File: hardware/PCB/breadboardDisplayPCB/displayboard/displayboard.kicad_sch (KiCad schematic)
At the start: 46 parts, among them J1 Conn_01x09_Socket, Q1 2N7000, U1 74HC595, U2 74HC595, U3 74HC595, U4 74HC595, U5 74HC595, U6 TBD62783A, U7 TBD62783A, U8 ULN2803A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

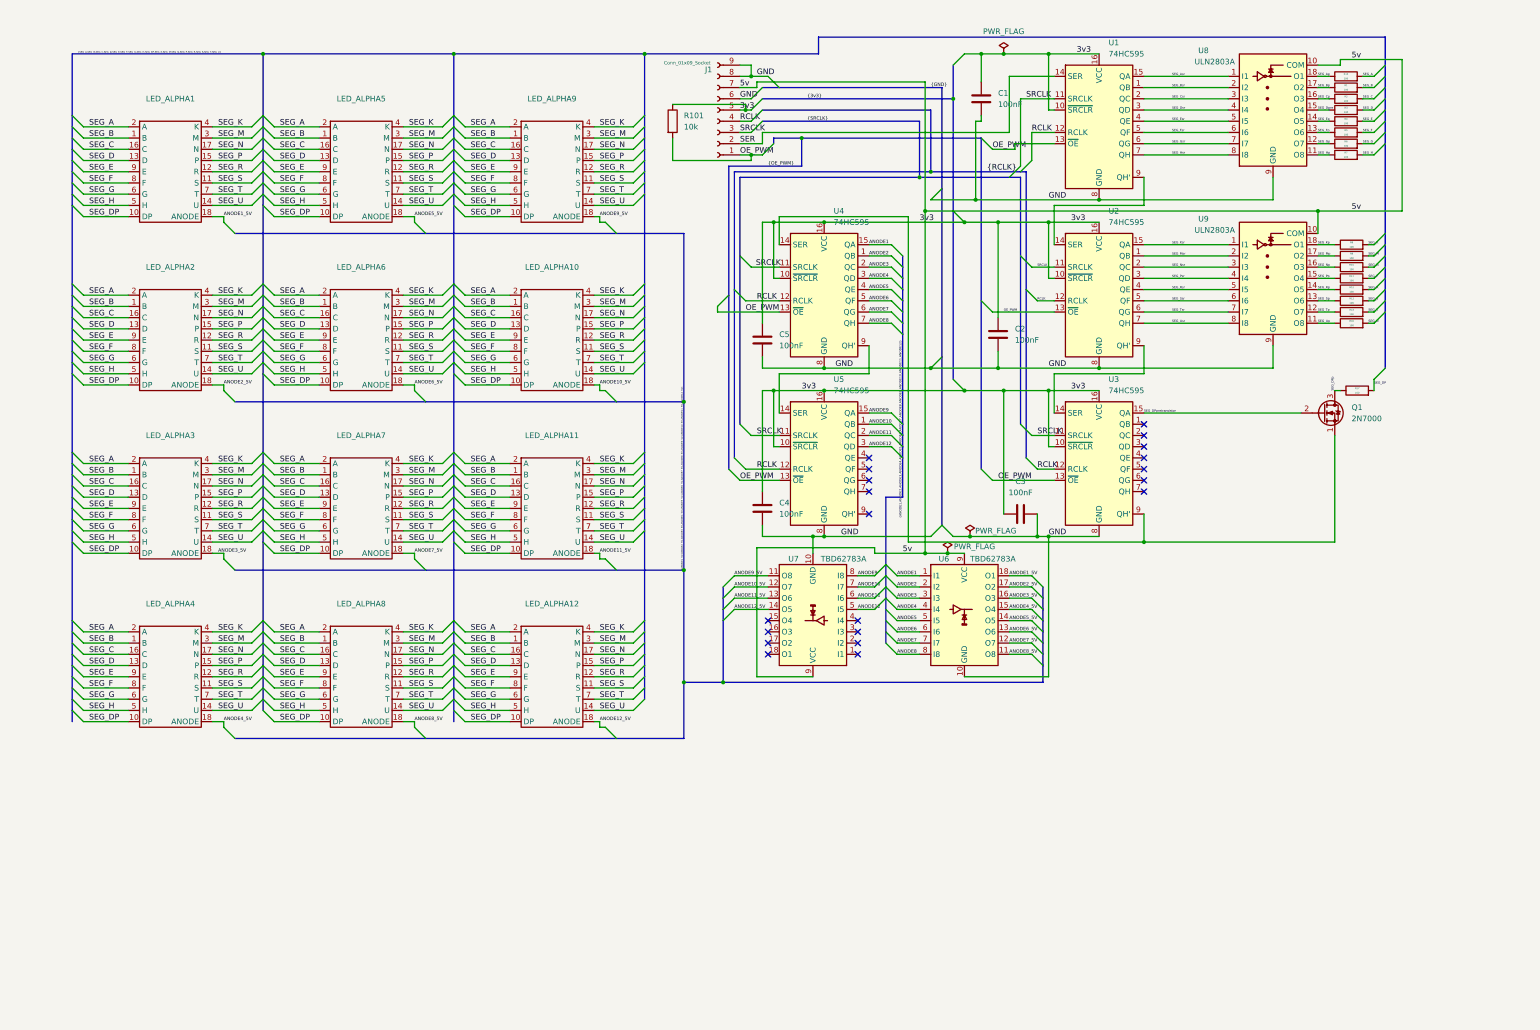
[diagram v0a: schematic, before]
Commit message: begin work on final display PCB
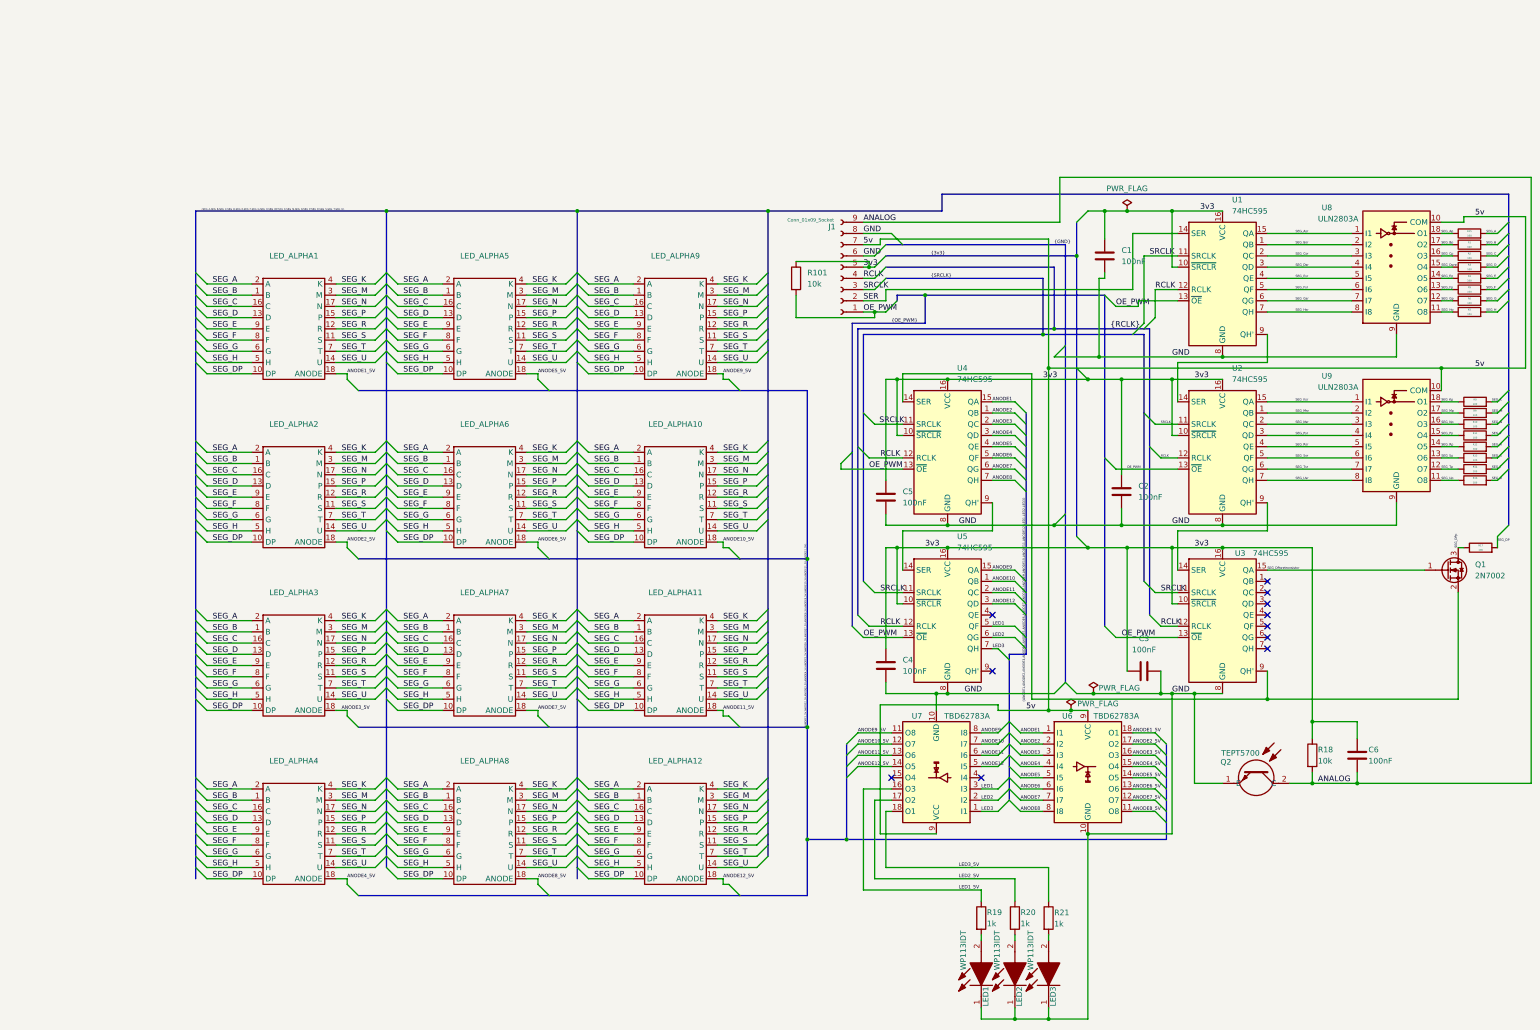
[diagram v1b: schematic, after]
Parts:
- removed Q1: 2N7000, Package_TO_SOT_THT:TO-92_Inline, symbol Transistor_FET:2N7000
- added C6: 100nF, Capacitor_SMD:C_0603_1608Metric, symbol Device:C
- added LED1, LED2, LED3: WP113IDT, SamacSys_Parts:WP113IDT, symbol SamacSys_Parts:WP113IDT
- added Q1: 2N7002, Package_TO_SOT_SMD:SOT-23, symbol Transistor_FET:2N7002
- added Q2: TEPT5700, SamacSys_Parts:TEPT5700, symbol SamacSys_Parts:TEPT5700
- added R18: 10k, Resistor_SMD:R_0805_2012Metric, symbol Device:R
- added R19, R20, R21: 1k, Resistor_SMD:R_0603_1608Metric, symbol Device:R
- C1, C2, C3, C4, C5: footprint Capacitor_THT:C_Disc_D5.0mm_W2.5mm_P5.00mm -> Capacitor_SMD:C_0603_1608Metric
- J1: footprint Connector_PinHeader_2.54mm:PinHeader_1x09_P2.54mm_Vertical -> Connector_JST:JST_XH_B9B-XH-A_1x09_P2.50mm_Vertical
- R1, R10, R11, R12, R13, R14, R15, R16, R17, R2, R3, R4, R5, R6, R7, R8, R9: footprint Resistor_THT:R_Axial_DIN0207_L6.3mm_D2.5mm_P7.62mm_Horizontal -> Resistor_SMD:R_0805_2012Metric
- R101: footprint Resistor_THT:R_Axial_DIN0207_L6.3mm_D2.5mm_P7.62mm_Horizontal -> Resistor_SMD:R_0603_1608Metric
- U1, U2, U3, U4, U5: footprint Package_DIP:DIP-16_W7.62mm_Socket -> Package_SO:SOIC-16_3.9x9.9mm_P1.27mm
- U6, U7, U8, U9: footprint Package_DIP:DIP-18_W7.62mm_Socket -> Package_SO:SOIC-18W_7.5x11.6mm_P1.27mm
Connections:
- net 3v3: now also C6.1, R18.1
- net GND: now also LED1.1 (K), LED2.1 (K), LED3.1 (K), Q2.1 (E); no longer J1.9 (Pin_9)
- net SEG_DPp: now also Q1.3 (D)
- net SEG_DPpretransistor: now also Q1.1 (G)
- net at U3.9 (QH'), U4.14 (SER): now also Q1.2 (S)
- net LED3: now reaches U7.1 (I1)
- net LED3: now also U5.7 (QH)
- net LED1_5V: now reaches U7.16 (O3)
- net LED1_5V: now also R19.1
- net LED2_5V: now reaches U7.17 (O2)
- net LED2_5V: now also R20.1
- net LED3_5V: now reaches U7.18 (O1)
- net LED3_5V: now also R21.1
- net LED2: now reaches U7.2 (I2)
- net LED2: now also U5.6 (QG)
- net LED1: now reaches U7.3 (I3)
- net LED1: now also U5.5 (QF)
- new net: LED1.2 (A), R19.2
- new net: LED3.2 (A), R21.2
- new net: LED2.2 (A), R20.2
- new net ANALOG: C6.2, J1.9 (Pin_9), Q2.2 (C), R18.2
- no-connect marks 20 -> 11
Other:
- moved on the sheet: C1, C2, C3, C4, C5, J1, LED_ALPHA1, LED_ALPHA10, LED_ALPHA11, LED_ALPHA12, LED_ALPHA2, LED_ALPHA3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

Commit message: final PCB rev work
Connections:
- net GND: now also Q1.2 (S)
- net at U3.9 (QH'), U4.14 (SER): no longer Q1.2 (S)
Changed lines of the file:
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@@
 	)
 	(junction
-		(at 224.79 96.52)
+		(at 287.02 167.64)
 		(diameter 0)
 		(color 0 0 0 0)
 	)
 	(junction
-		(at 260.35 58.42)
+		(at 224.79 96.52)
 		(diameter 0)
 		(color 0 0 0 0)
 	)
 	(junction
-		(at 254 68.58)
+		(at 260.35 58.42)
 		(diameter 0)
 		(color 0 0 0 0)
 	)
 	(junction
-		(at 297.18 168.91)
+		(at 254 68.58)
 		(diameter 0)
 		(color 0 0 0 0)
@@
 	(wire
 		(pts
+			(xy 340.36 144.78) (xy 340.36 167.64)
+		)
+		(stroke
+			(width 0)
+			(type default)
+		)
+	)
+	(wire
+		(pts
 			(xy 264.16 125.73) (xy 264.16 129.54)
 		)
@@
 	(wire
 		(pts
+			(xy 340.36 167.64) (xy 287.02 167.64)
+		)
+		(stroke
+			(width 0)
+			(type default)
+		)
+	)
+	(wire
+		(pts
 			(xy 86.36 74.93) (xy 95.25 74.93)
 		)
@@
 	(wire
 		(pts
-			(xy 297.18 168.91) (xy 340.36 168.91)
-		)
-		(stroke
-			(width 0)
-			(type default)
-		)
-	)
-	(wire
-		(pts
 			(xy 287.02 187.96) (xy 280.67 187.96)
 		)
@@
 		)
 		(stroke
-			(width 0)
-			(type default)
-		)
-	)
-	(wire
-		(pts
-			(xy 340.36 144.78) (xy 340.36 168.91)
-		)
-		(stroke

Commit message: large commit of PCB progress
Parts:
- added C7: 47uF, Capacitor_SMD:CP_Elec_6.3x5.4, symbol Device:C_Polarized
- C1, C2, C3, C6: LCSC (none) -> C14663
- C4: renamed from C5; LCSC (none) -> C14663
- C5: renamed from C4; LCSC (none) -> C14663
- J1, LED1, LED2, LED3, LED_ALPHA1, LED_ALPHA12, Q2: now left out of the parts list
- LED_ALPHA10: renamed from LED_ALPHA4; now left out of the parts list
- LED_ALPHA11: renamed from LED_ALPHA8; now left out of the parts list
- LED_ALPHA2: renamed from LED_ALPHA5; now left out of the parts list
- LED_ALPHA3: renamed from LED_ALPHA9; now left out of the parts list
- LED_ALPHA4: renamed from LED_ALPHA2; now left out of the parts list
- LED_ALPHA5: renamed from LED_ALPHA6; now left out of the parts list
- LED_ALPHA6: renamed from LED_ALPHA10; now left out of the parts list
- LED_ALPHA7: renamed from LED_ALPHA3; now left out of the parts list
- LED_ALPHA8: renamed from LED_ALPHA7; now left out of the parts list
- LED_ALPHA9: renamed from LED_ALPHA11; now left out of the parts list
- Q1: LCSC (none) -> C8545
- R1, R10, R11, R12, R13, R14, R15, R16, R17, R2, R3, R4, R5, R6, R7, R8, R9: LCSC (none) -> C17467
- R101: LCSC (none) -> C25804
- R18: LCSC (none) -> C17414
- R19, R20, R21: LCSC (none) -> C21122
- U1, U2, U3, U4, U5: LCSC (none) -> C14791
- U6, U7: LCSC (none) -> C96336
- U8, U9: value ULN2803A -> TBD62083A; LCSC (none) -> C134547
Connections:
- net ANODE10: now also U7.2 (I2); no longer U7.7 (I7)
- net ANODE10_5V: now also LED_ALPHA10.18 (ANODE), U7.17 (O2); no longer LED_ALPHA6.18 (ANODE), U7.12 (O7)
- net ANODE11: now also U7.3 (I3); no longer U7.6 (I6)
- net ANODE11_5V: now also LED_ALPHA11.18 (ANODE), U7.16 (O3); no longer LED_ALPHA9.18 (ANODE), U7.13 (O6)
- net ANODE12: now also U7.4 (I4); no longer U7.5 (I5)
- net ANODE12_5V: now also U7.15 (O4); no longer U7.14 (O5)
- net ANODE2_5V: now also LED_ALPHA2.18 (ANODE); no longer LED_ALPHA4.18 (ANODE)
- net ANODE3_5V: now also LED_ALPHA3.18 (ANODE); no longer LED_ALPHA7.18 (ANODE)
- net ANODE4_5V: now also LED_ALPHA4.18 (ANODE); no longer LED_ALPHA10.18 (ANODE)
- net ANODE5_5V: now also LED_ALPHA5.18 (ANODE); no longer LED_ALPHA2.18 (ANODE)
- net ANODE6_5V: now also LED_ALPHA6.18 (ANODE); no longer LED_ALPHA5.18 (ANODE)
- net ANODE7_5V: now also LED_ALPHA7.18 (ANODE); no longer LED_ALPHA8.18 (ANODE)
- net ANODE8_5V: now also LED_ALPHA8.18 (ANODE); no longer LED_ALPHA11.18 (ANODE)
- net ANODE9: now also U7.1 (I1); no longer U7.8 (I8)
- net ANODE9_5V: now also LED_ALPHA9.18 (ANODE), U7.18 (O1); no longer LED_ALPHA3.18 (ANODE), U7.11 (O8)
- net GND: now also C2.1, C3.1, C4.2, C5.2, C7.2; no longer C2.2, C3.2, C4.1, C5.1
- net LED1: now also U7.6 (I6); no longer U7.3 (I3)
- net LED1_5V: now also U7.13 (O6); no longer U7.16 (O3)
- net LED2: now also U7.7 (I7); no longer U7.2 (I2)
- net LED2_5V: now also U7.12 (O7); no longer U7.17 (O2)
- net LED3: now also U7.8 (I8); no longer U7.1 (I1)
- net LED3_5V: now also U7.11 (O8); no longer U7.18 (O1)
- net ANODE_SER: now reaches U3.9 (QH'), U4.14 (SER)
- net 3v3 renamed +3V3
- net +3V3: now also C2.2, C3.2, C4.1, C5.1; no longer C2.1, C3.1, C4.2, C5.2
- net 5v renamed +5V
- net +5V: now also C7.1
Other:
- note added: "AMBIENT LIGHT SENSOR"
- note added: "ANODE/LED DRIVER"
- note added: "CONNECTOR"
- note added: "DISPLAY MATRIX"
- note added: "INDICATOR LEDS"
- note added: "SEGMENT DRIVER"
- company: (none) -> NATHANIEL KESSEL
- moved on the sheet: C1, C2, C3, C4, C5, C6, J1, LED1, LED2, LED3, LED_ALPHA1, LED_ALPHA10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

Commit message: KiCad 10 update, clock funtion fixes
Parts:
- LED_ALPHA1, LED_ALPHA10, LED_ALPHA11, LED_ALPHA12, LED_ALPHA2, LED_ALPHA3, LED_ALPHA4, LED_ALPHA5, LED_ALPHA6, LED_ALPHA7, LED_ALPHA8, LED_ALPHA9: value ~ -> (none)
